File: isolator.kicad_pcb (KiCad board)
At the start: 4 copper layers, 120 x 50 mm, 55 parts, among them J1 HOST, J2 ISO_PORT, Q1 2N7002, T1 750313638, U1 ADuM4165, U2 USBLC6-2SC6, U3 USBLC6-2SC6, U4 SN6505BDBV, U5 TLV76750DGNR, U6 TPS2553DBV, Y1 24M 8pF

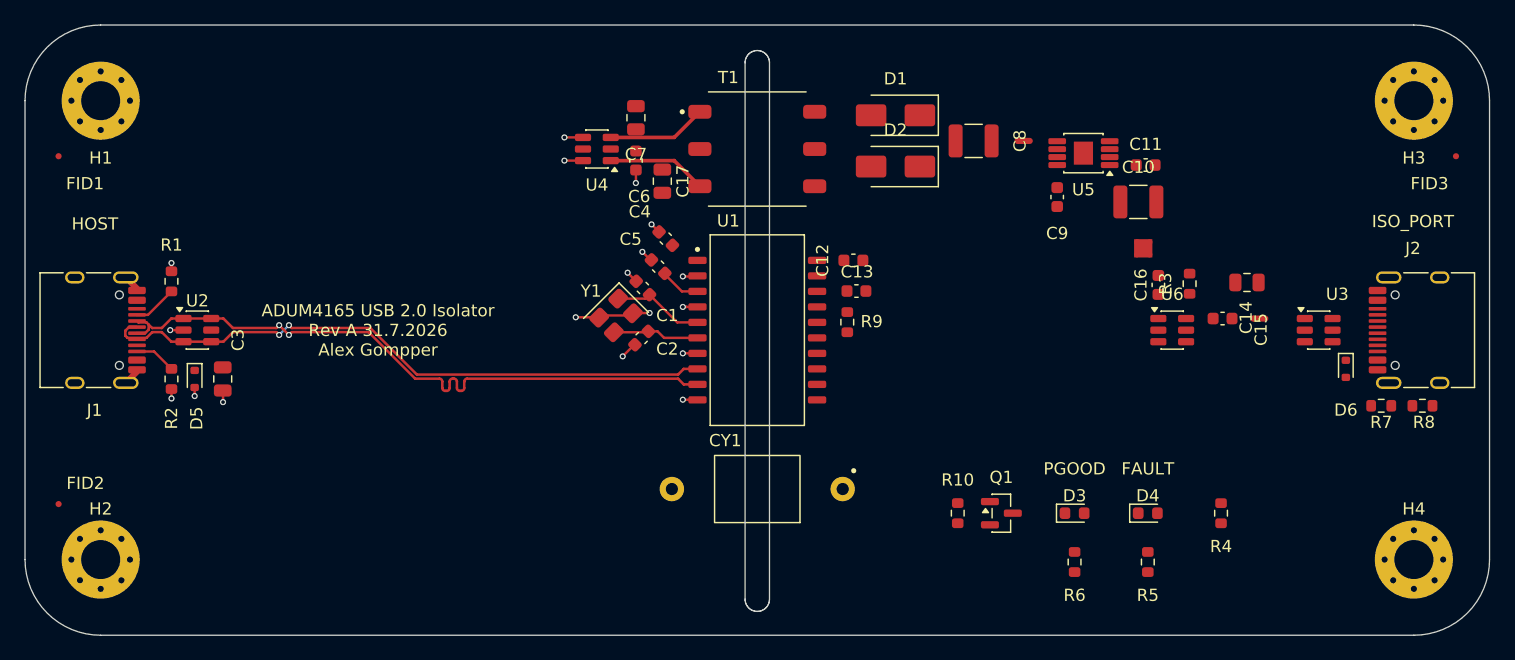
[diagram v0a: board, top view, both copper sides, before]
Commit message: feat(pcb): route the eight branch nets through their star points
Every branch reaches its trunk only through its net tie. Both pads of NT1,
NT2 and NT3 carry track copper, no tie pad is fed by a pour, and no via sits
on one. Measured min separation between each tie's two nets, board-wide, is
0.45-0.50 mm and always at the tie itself.

Three obstacles Task 4's review named:
- NT2.1 <- C8.1 goes around C8's own GND2 pad to the south (y 88.300, up at
  x 167.400, entering NT2.1 from the west).
- NT3.2 -> U3.5 climbs to y 99.350 north of U3 and drops into U3.5 down the
  0.95 mm gap between U3's pad columns, leaving x 194.675..196.975 free for
  Task 6's pair. D6/J2.A4/R7/R8 are reached under that lane on B.Cu.
- NT1.4's pinch: /ISO_5V_IND leaves straight south 0.8 mm and drops to B.Cu,
  which also clears /ISO_5V_SW's lane and the /PORT_D+- corridor (the same
  B.Cu crossing 2c1167d used).

/VBUS_HOST rebuilt from scratch: the J1 -> D5/C3/U2.5 -> U4 -> C4/U1.1
topology restored from 2c1167d, plus B.Cu hops for C7 and C17, both of which
Task 4's placement fenced behind the /PP_A and /PP_B windings.

Also removes 72 orphaned teardrop ZONES -- floating copper Task 3's rip left
behind, four of them sitting in the NT2 -> U5 corridor. A teardrop is removed
only when no pad, track or via of its own net touches it, so this cannot
change connectivity.

DRC: 22 violations, byte-for-byte the same 22 the board had before this
commit (2 pre-existing /PP_A|/PP_B clearance errors from Task 4's C7/C17
placement, 20 silkscreen). Unconnected 90 -> 51, with zero on all nine nets.
Gates 1, 2, 5, netclass coverage and decoupling nets all PASS.

Co-Authored-By: Claude Opus 5 <noreply@anthropic.com>
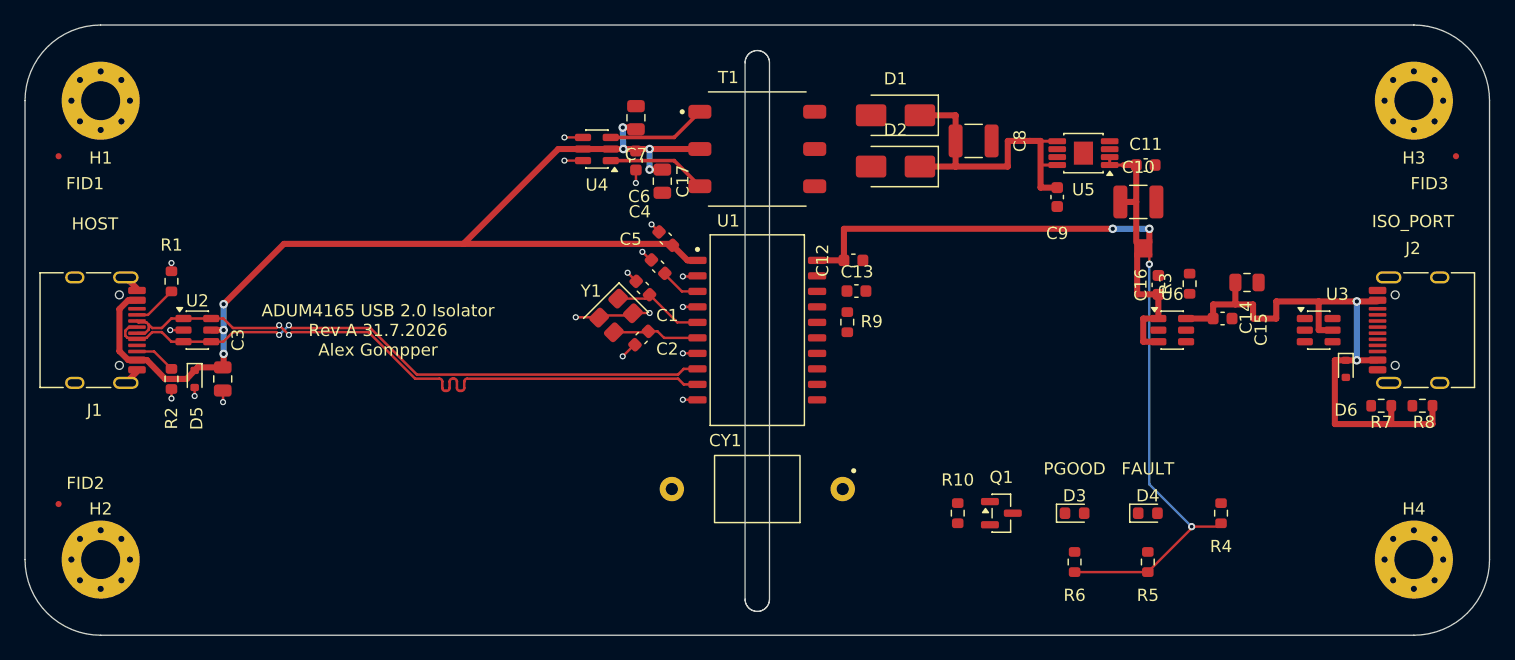
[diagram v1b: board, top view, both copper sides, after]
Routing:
- net /VBUS_HOST: track 0.00 -> 90.6 mm, vias 0 -> 7
- net /PORT_VBUS_J2: track 0.00 -> 38.6 mm, vias 0 -> 2
- net /ISO_5V_IND: track 0.00 -> 37.5 mm, vias 0 -> 2
- net /ISO_5V_VBUS2: track 0.00 -> 30.9 mm, vias 0 -> 2
- net /DCDC_RECT: track 0.00 -> 17.2 mm
- net /ISO_5V_SW: track 0.00 -> 11.4 mm
- net /ISO_5V: track 0.00 -> 10.5 mm
- net /PORT_VBUS: track 0.00 -> 9.59 mm
- net /DCDC_RAW: track 0.00 -> 8.80 mm

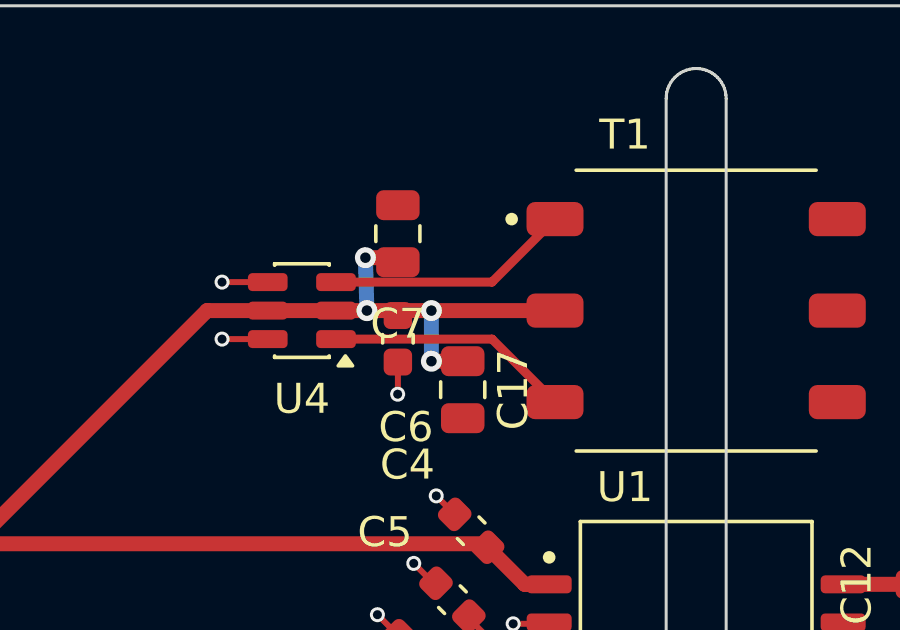
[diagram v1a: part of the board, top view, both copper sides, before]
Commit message: fix(pcb): nudge C7 and C17 clear of the /PP_A and /PP_B windings
Both caps sat inside DRC clearance of the frozen transformer primary drive as
Task 4 placed them -- a track-to-PAD conflict a courtyard check cannot see:

  C7.1  y 84.750..85.750 vs /PP_B edges 85.7634..86.0634 -> 0.0134 mm
  C17.1 y 88.050..89.050 vs /PP_A edges 87.6634..87.9634 -> 0.0866 mm

against a 0.15 mm PWR clearance. C7 moves north 0.20 mm, C17 south 0.12 mm,
measured 0.2134 and 0.2066 mm after. Ruling: move the capacitors, do not
re-route /PP_A or /PP_B.

DRC [clearance] violations 2 -> 0, and no new one anywhere on the board.
Total 22 -> 19, the remainder all silkscreen; diffed the silk list, one
overlap cleared and none created. Courtyards: 0 overlaps across 1326 pairs.
decoupling.py PASS on all 17 rows (C7 2.75, C17 3.57, C6 still inboard).
Gates 1 and 2 PASS unchanged. Ratsnest still zero on all nine nets.

Board rebuilt from the Task-4 state through place_iso.py then route_iso.py so
the pipeline stays reproducible; route_iso.py's four /VBUS_HOST waypoints into
C7.1 and C17.1 retargeted to the new pad centres.

Correcting one claim in the ruling, measured both ways: C7's lift does NOT
relax the C7<->U4 courtyard gap. That is 0.1800 mm before and after, and
C17<->T1 is 0.2110 mm before and after -- both are pure dx. C6<->C7 is what
relaxes, 0.3334 -> 0.5334 mm.

Co-Authored-By: Claude Opus 5 <noreply@anthropic.com>
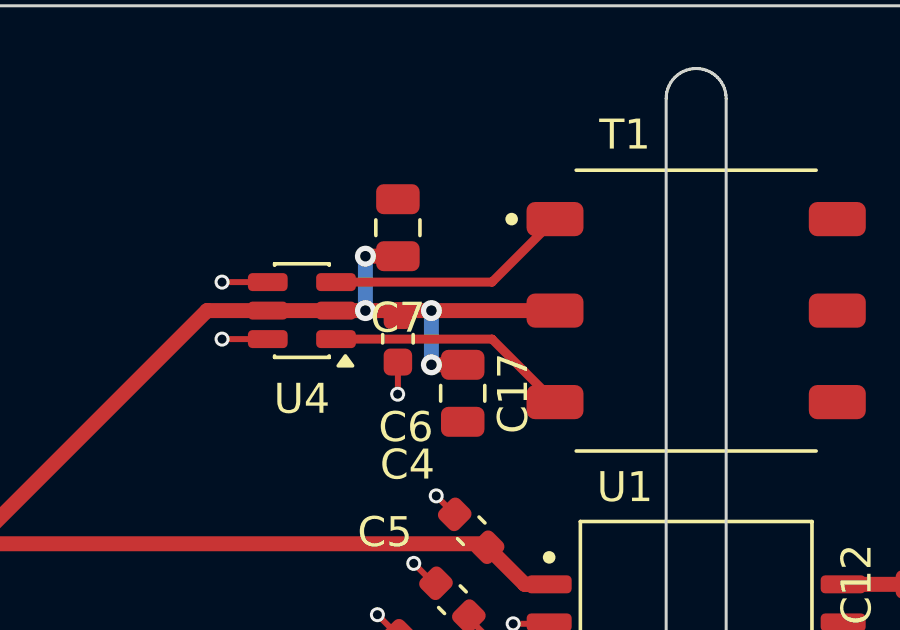
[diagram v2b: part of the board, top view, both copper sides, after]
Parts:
- moved C7 0.20 mm to (136.9, 84.1)
- moved C17 0.12 mm to (139.1, 89.6)

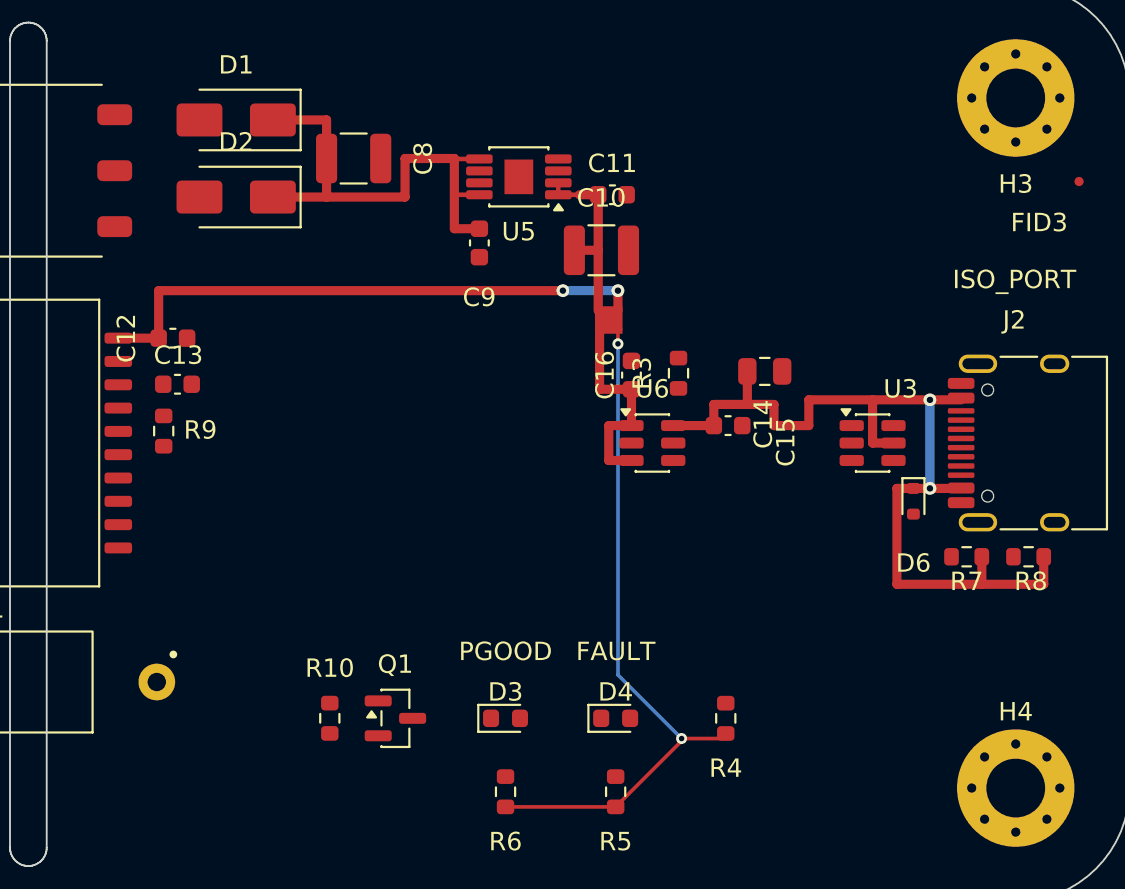
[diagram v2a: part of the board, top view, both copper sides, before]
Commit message: feat(pcb): route PORT_D+/- matched and the remaining isolated-side signals
/PORT_D+- comes back at 0.21/0.127, 90 ohm class, with Gate 3 reporting
0.0001 mm intra-pair skew. The F.Cu backbone is 2c1167d's -- U1, U3 and J2
never moved -- with two changes:

  * the crossover is rebuilt symmetrically at x 167.225..169.225, so it is
    length-neutral by construction rather than by luck;
  * U3.1 -> U3.6 can no longer run straight across the gap between U3's pad
    columns. Task 5 routes /PORT_VBUS_J2 down that 0.95 mm gap to reach U3.5,
    and neither side of it leaves the 0.505 mm a 0.21 mm trace needs. D+ hops
    it on 1.45 mm of B.Cu north of the pad row instead. The eight power nets
    were not touched to make room.

D- carries a three-tooth 45 degree serpentine that pays back the 0.7235 mm the
hop and the fan-out cost D+. Its amplitude is solved, not guessed:
route_signals.py --tune prints it.

/HOST_D+- is untouched and still reports its pre-existing 2.9092 mm, so Gate 3's
overall verdict is still FAIL. That is the accepted end state.

Also routed: /RECT_A, /RECT_B, /ILIM_SET, /nFAULT, /PGOOD2, /VDD2, /PG_LED_A,
/PG_LED_K, /FAULT_LED_A, /PORT_CC1, /PORT_CC2. The signals whose parts did not
move are restored from 2c1167d and re-checked against Task 4 and 5's copper;
/RECT_A/B and /ILIM_SET are new because D1, D2 and R3 all moved.

Ratsnest is down from 48 to 26, and every remaining item is GND1/GND2 reaching
its inner plane -- Task 7's stitching, not this task's.

Co-Authored-By: Claude Opus 5 <noreply@anthropic.com>
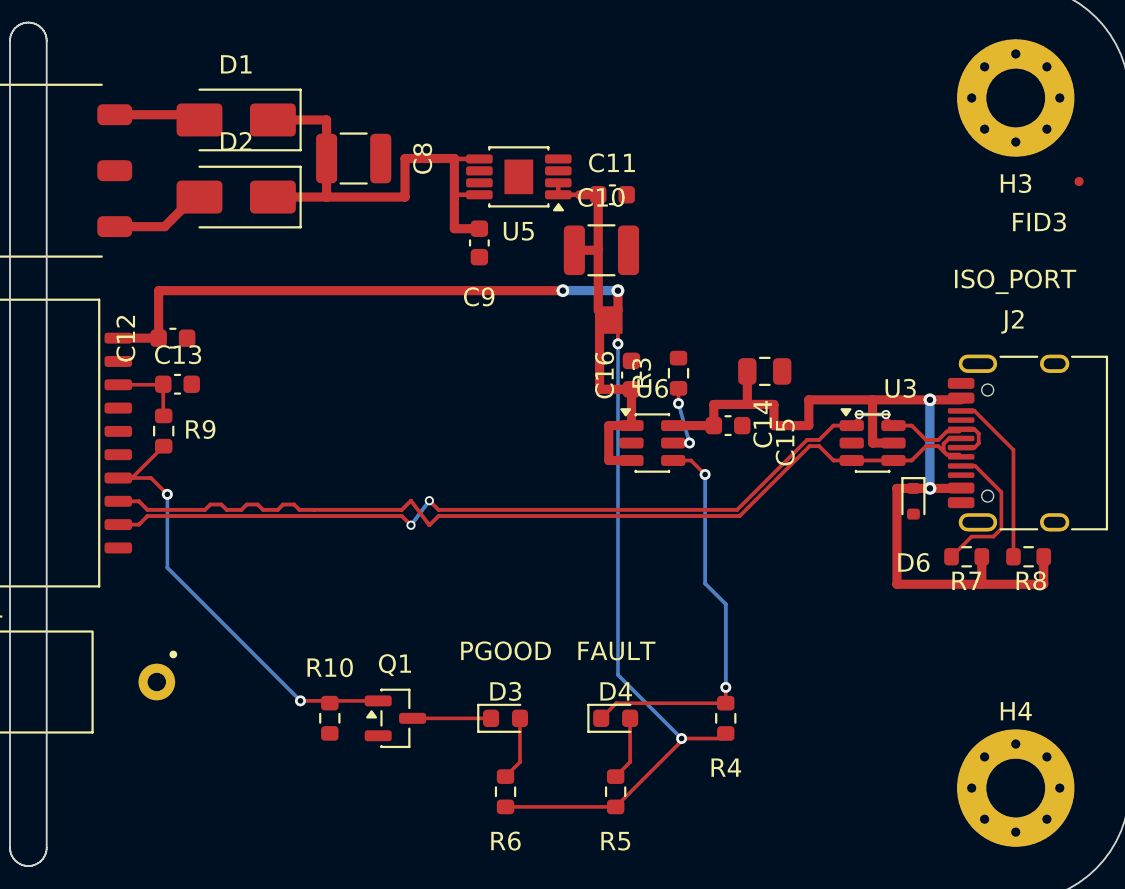
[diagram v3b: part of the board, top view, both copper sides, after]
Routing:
- net /PORT_D+: track 0.00 -> 53.0 mm, vias 0 -> 4
- net /PORT_D-: track 0.00 -> 51.9 mm
- net /PGOOD2: track 0.00 -> 23.7 mm, vias 0 -> 2
- net /nFAULT: track 0.00 -> 22.1 mm, vias 0 -> 2
- net /PORT_CC2: track 0.00 -> 9.55 mm
- net /PORT_CC1: track 0.00 -> 8.13 mm
- net /RECT_B: track 0.00 -> 5.29 mm
- net /RECT_A: track 0.00 -> 4.62 mm
- net /PG_LED_K: track 0.00 -> 4.28 mm
- net /VDD2: track 0.00 -> 4.12 mm
- net /ILIM_SET: track 0.00 -> 3.95 mm, vias 0 -> 2
- net /PG_LED_A: track 0.00 -> 3.50 mm
- net /FAULT_LED_A: track 0.00 -> 3.50 mm

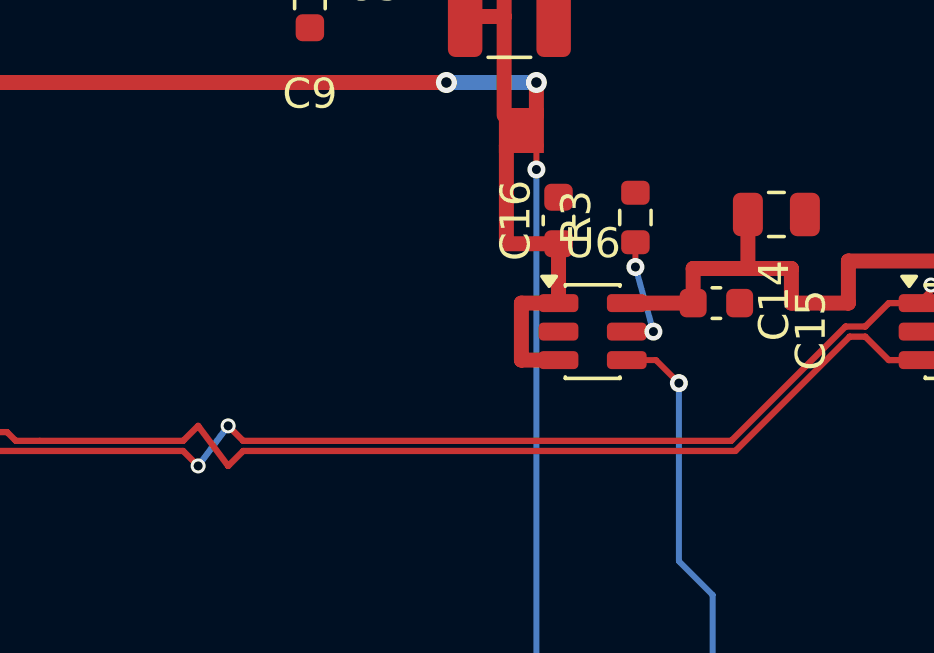
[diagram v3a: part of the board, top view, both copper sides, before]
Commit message: fix(pcb): make PORT_D+/- structurally symmetric, move R3 for ILIM_SET
The pair matched at 0.0001 mm skew but was built asymmetrically: D+ carried
4 vias and 3.12 mm of B.Cu while D- stayed on F.Cu. Leg asymmetry is what
converts differential into common mode, so that optimised the number the gate
measures over the thing it protects.

A planar crossing forces exactly one conductor onto the other layer, but not
which one. D+ already carries a forced 2-via, 1.450 mm B.Cu hop over
/PORT_VBUS_J2's trunk at U3, so the crossover dip moves to D- and its diagonal
is sized to 1.450 mm exactly. Both legs now read 2 vias, 1.4500 mm B.Cu and
48.5680 mm F.Cu on the measured path. Skew 0.0001 mm, Zdiff [OK].

R3 moves from (182.300, 97.900) rot 90 to (185.000, 102.450) rot 0, onto the
same side of /PORT_VBUS's trunk as U6.5. /ILIM_SET becomes 2.4716 mm of F.Cu
with no vias, down from 3.9440 mm with two -- SLVS841F Sec 8.3.3 is explicit
that parasitics there degrade current-limit accuracy.

Board rebuilt from 8602e81 through place_iso.py, route_iso.py, route_signals.py
because R3 moving is a placement change. The eight power nets, /VBUS_HOST and
/HOST_D+/- are item-for-item identical to ea339c4; R3 is the only footprint that
differs. Gates 1, 2 and 5 pass, decoupling.py on all 17 rows; 0 courtyard
overlaps over 1326 pairs; DRC 19 -> 18, the delta being R3's reference
designator moving off C16 onto C15.

Co-Authored-By: Claude Opus 5 <noreply@anthropic.com>
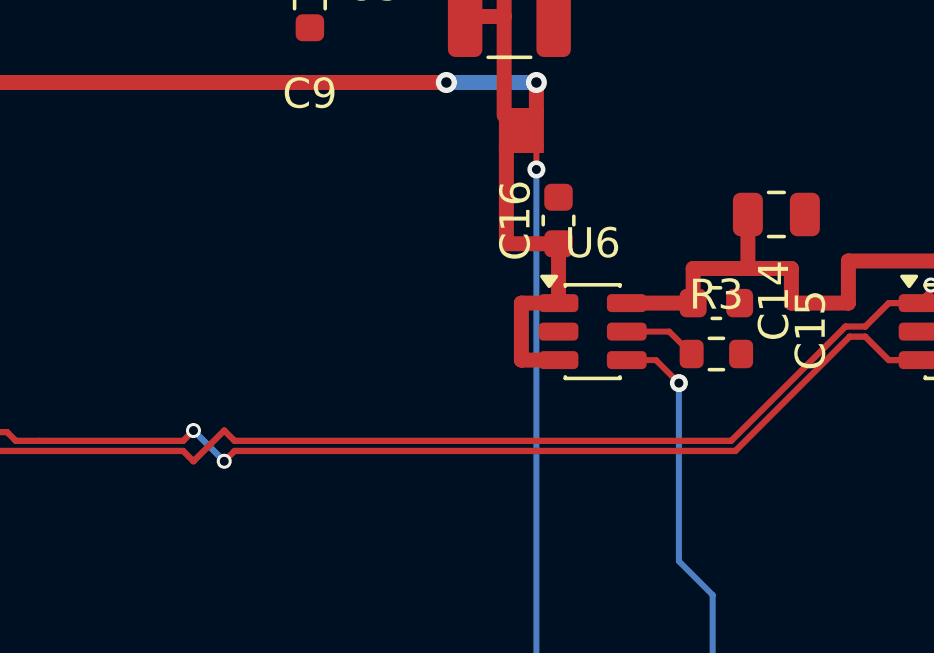
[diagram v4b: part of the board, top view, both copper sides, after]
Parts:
- moved R3 5.29 mm to (185.0, 102.5), turned to 0 degrees
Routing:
- net /ILIM_SET: track 3.95 -> 2.47 mm, vias 2 -> 0
- net /PORT_D-: track 51.9 -> 51.5 mm, vias 0 -> 2
- net /PORT_D+: track 53.0 -> 52.7 mm, vias 4 -> 2
